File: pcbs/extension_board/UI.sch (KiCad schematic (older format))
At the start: 21 parts, among them J8 Conn_01x08, SW1 MY_SW_Push_Dual, SW2 Rotary_Encoder, SW3 Rotary_Encoder

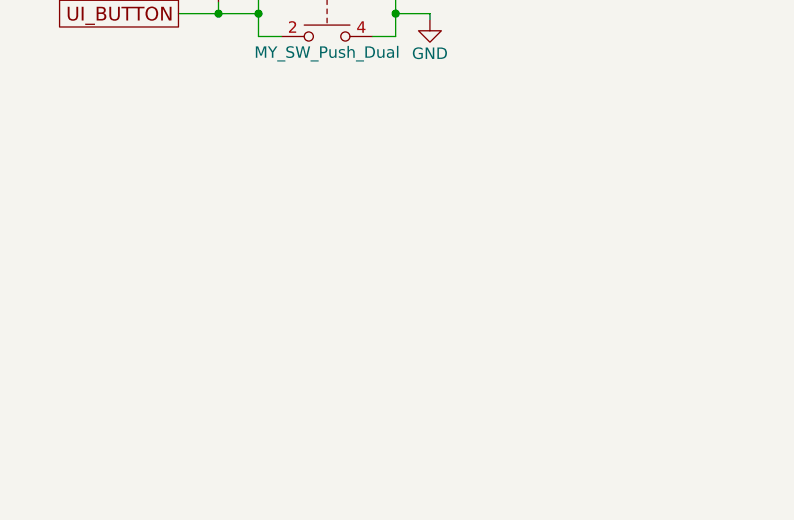
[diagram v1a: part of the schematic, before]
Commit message: osPrintf works with signed and unsigned integers.
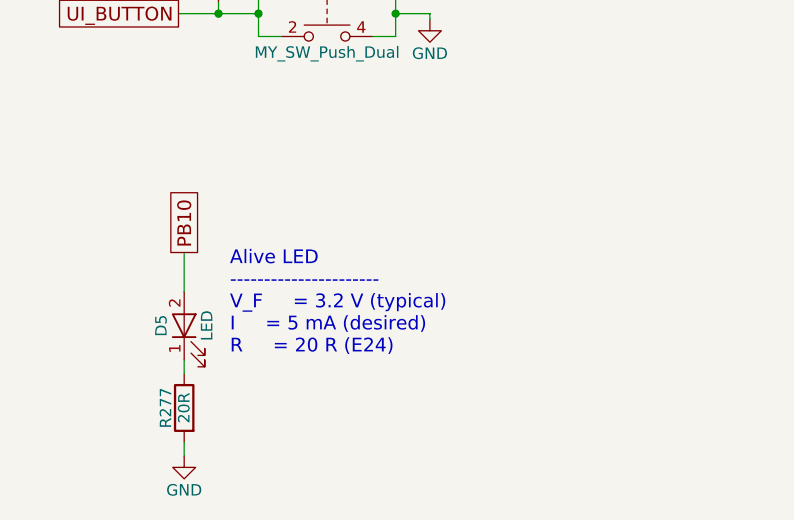
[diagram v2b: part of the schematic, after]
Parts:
- added D5: LED, LEDs:LED_0603, symbol LED
- added R277: 20R, Resistors_SMD:R_0603, symbol R
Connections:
- net GND: now also R277.2
- new net: D5.1 (K), R277.1
- new net PB10: D5.2 (A)
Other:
- note added: "Alive LED\n----------------------\nV_F = 3.2 V (typical)\nI = 5 mA (desired)\nR = 20 R (E24)"
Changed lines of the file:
@@
 Connection ~ 3125 4550
 $Comp
-L GND #PWR0300
+L GND #PWR299
 U 1 1 5A0B85D7
 P 3875 4575
-F 0 "#PWR0300" H 3875 4325 50  0001 C CNN
+F 0 "#PWR299" H 3875 4325 50  0001 C CNN
 F 1 "GND" H 3875 4425 50  0000 C CNN
 F 2 "" H 3875 4575 50  0001 C CNN
@@
 Connection ~ 2950 4550
 $Comp
-L GND #PWR0301
+L GND #PWR303
 U 1 1 5A0B9013
 P 8075 4125
-F 0 "#PWR0301" H 8075 3875 50  0001 C CNN
+F 0 "#PWR303" H 8075 3875 50  0001 C CNN
 F 1 "GND" H 8075 3975 50  0000 C CNN
 F 2 "" H 8075 4125 50  0001 C CNN
@@
 $EndComp
 $Comp
-L GND #PWR0302
+L GND #PWR305
 U 1 1 5A0BA939
 P 8825 4850
-F 0 "#PWR0302" H 8825 4600 50  0001 C CNN
+F 0 "#PWR305" H 8825 4600 50  0001 C CNN
 F 1 "GND" H 8825 4700 50  0000 C CNN
 F 2 "" H 8825 4850 50  0001 C CNN
@@
 $EndComp
 $Comp
-L GND #PWR0303
+L GND #PWR301
 U 1 1 5A0BE4A9
 P 6975 4850
-F 0 "#PWR0303" H 6975 4600 50  0001 C CNN
+F 0 "#PWR301" H 6975 4600 50  0001 C CNN
 F 1 "GND" H 6975 4700 50  0000 C CNN
 F 2 "" H 6975 4850 50  0001 C CNN
@@
 $EndComp
 $Comp
-L GND #PWR0304
+L GND #PWR302
 U 1 1 5A0E5835
 P 8020 2555
-F 0 "#PWR0304" H 8020 2305 50  0001 C CNN
+F 0 "#PWR302" H 8020 2305 50  0001 C CNN
 F 1 "GND" H 8020 2405 50  0000 C CNN
 F 2 "" H 8020 2555 50  0001 C CNN
@@
 $EndComp
 $Comp
-L GND #PWR0305
+L GND #PWR304
 U 1 1 5A0E584B
 P 8770 3280
-F 0 "#PWR0305" H 8770 3030 50  0001 C CNN
+F 0 "#PWR304" H 8770 3030 50  0001 C CNN
 F 1 "GND" H 8770 3130 50  0000 C CNN
 F 2 "" H 8770 3280 50  0001 C CNN
@@
 $EndComp
 $Comp
-L GND #PWR0306
+L GND #PWR300
 U 1 1 5A0E5872
 P 6920 3280
-F 0 "#PWR0306" H 6920 3030 50  0001 C CNN
+F 0 "#PWR300" H 6920 3030 50  0001 C CNN
 F 1 "GND" H 6920 3130 50  0000 C CNN
 F 2 "" H 6920 3280 50  0001 C CNN
@@
 Text GLabel 2800 2850 0    47   UnSpc ~ 0
 SPI_MISO
+$Comp
+L LED D5
+U 1 1 5A2A7A98
+P 2800 5915
+F 0 "D5" H 2800 6015 50  0000 C CNN
+F 1 "LED" H 2800 5815 50  0000 C CNN
+F 2 "LEDs:LED_0603" H 2800 5915 50  0001 C CNN
+F 3 "http://katalog.we-online.de/led/datasheet/150060GS75000.pdf" H 2800 5915 50  0001 C CNN
+F 4 "732-4971-1-ND" H 2800 5915 60  0001 C CNN "Digikey"
+	1    2800 5915
+	0    -1   -1   0
+$EndComp
+$Comp
+L R R277
+U 1 1 5A2A7AA0
+P 2800 6275
+F 0 "R277" V 2880 6275 50  0000 C CNN
+F 1 "20R" V 2800 6275 50  0000 C CNN
+F 2 "Resistors_SMD:R_0603" V 2730 6275 50  0001 C CNN
+F 3 "" H 2800 6275 50  0001 C CNN
+F 4 "1276-6153-1-ND" V 2800 6275 60  0001 C CNN "Digikey"
+	1    2800 6275
+	-1   0    0    -1
+$EndComp
+$Comp
+L GND #PWR298
+U 1 1 5A2A7AA7
+P 2800 6485
+F 0 "#PWR298" H 2800 6235 50  0001 C CNN
+F 1 "GND" H 2800 6335 50  0000 C CNN
+F 2 "" H 2800 6485 50  0001 C CNN
+F 3 "" H 2800 6485 50  0001 C CNN
+	1    2800 6485
+	1    0    0    -1
+$EndComp
+Text GLabel 2800 5595 1    60   UnSpc ~ 0
+PB10
+Text Notes 3000 6045 0    60   ~ 0
+Alive LED\n----------------------\nV_F 	= 3.2 V (typical)\nI 	= 5 mA (desired)\nR 	= 20 R (E24)
+Wire Wire Line
+	2800 6425 2800 6485
+Wire Wire Line
+	2800 6125 2800 6065
+Wire Wire Line
+	2800 5595 2800 5765
 $EndSCHEMATC
